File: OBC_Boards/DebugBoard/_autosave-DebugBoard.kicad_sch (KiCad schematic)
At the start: 15 parts, among them J1 Conn_01x02_Female, J2 Conn_02x06_Counter_Clockwise, J3 Conn_01x03, P1 USB_C_Plug_USB2.0, U1 L102021MS02Q

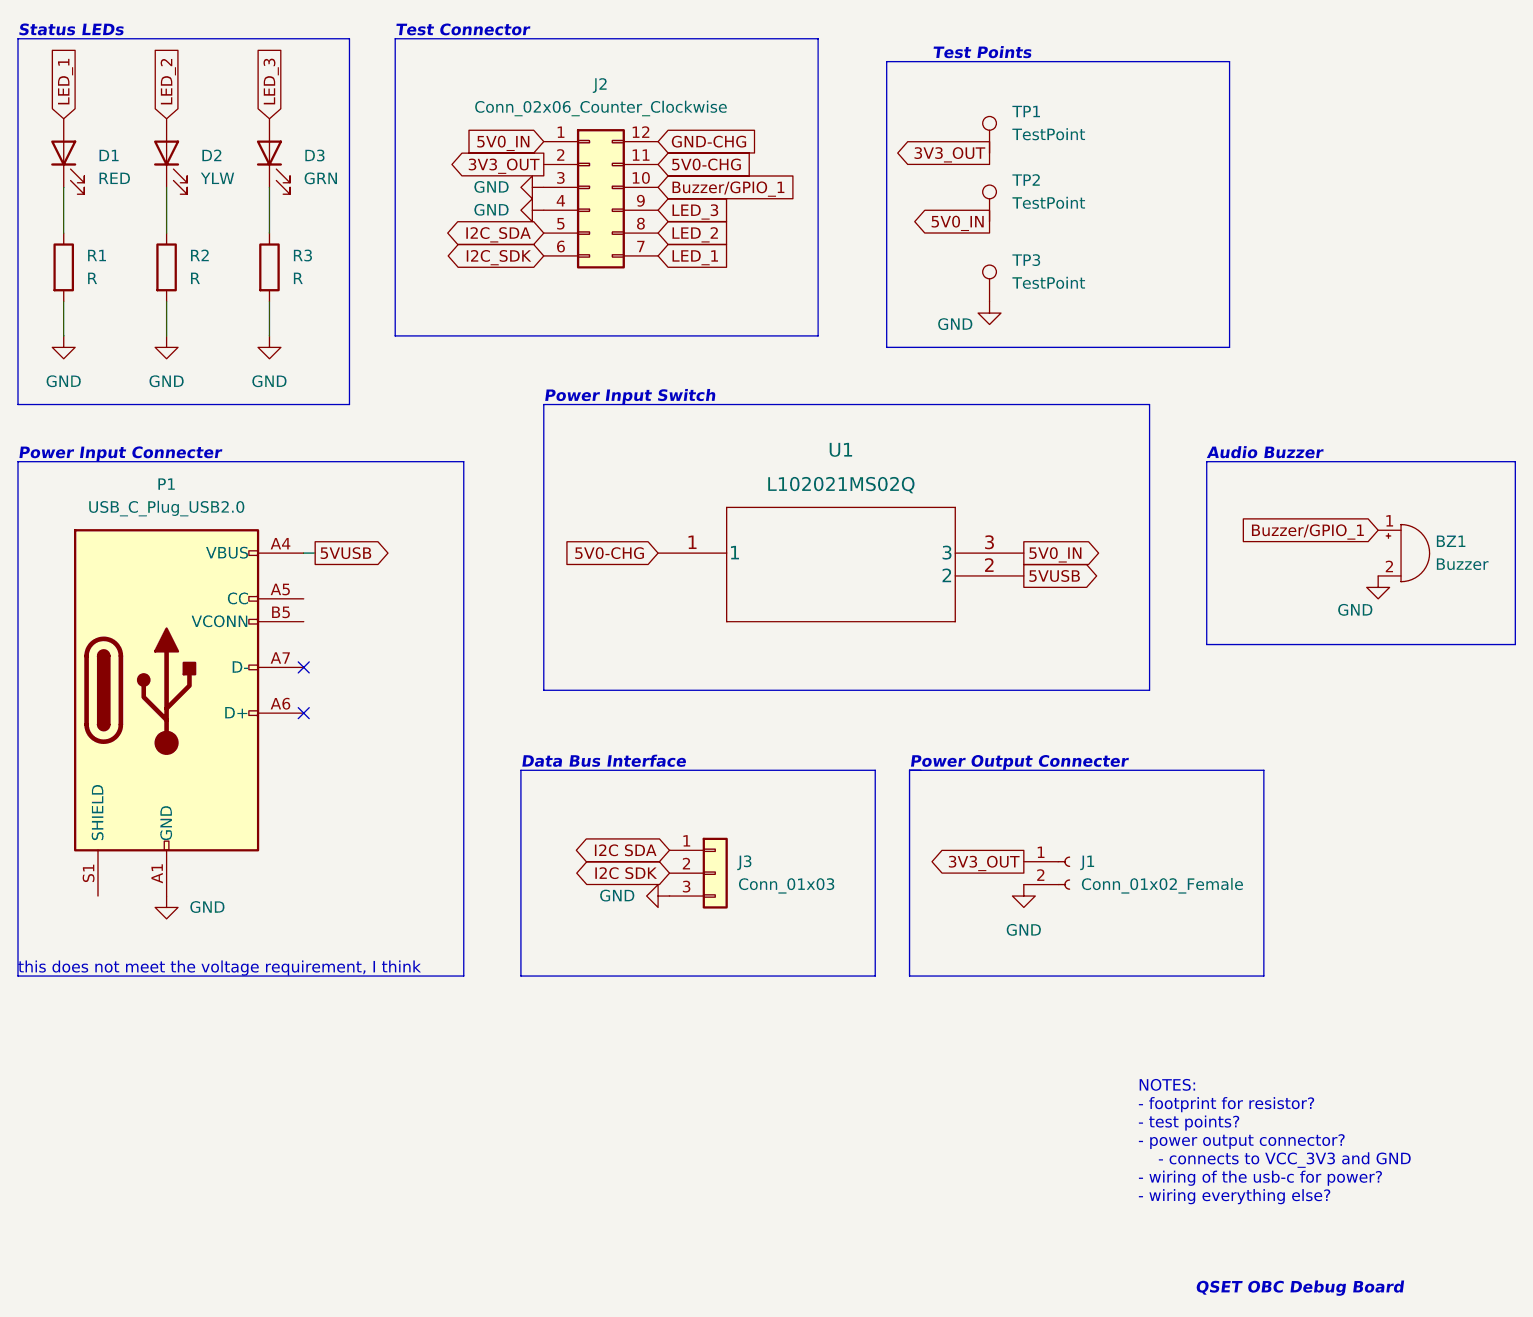
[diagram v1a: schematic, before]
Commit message: Created Debug PCB
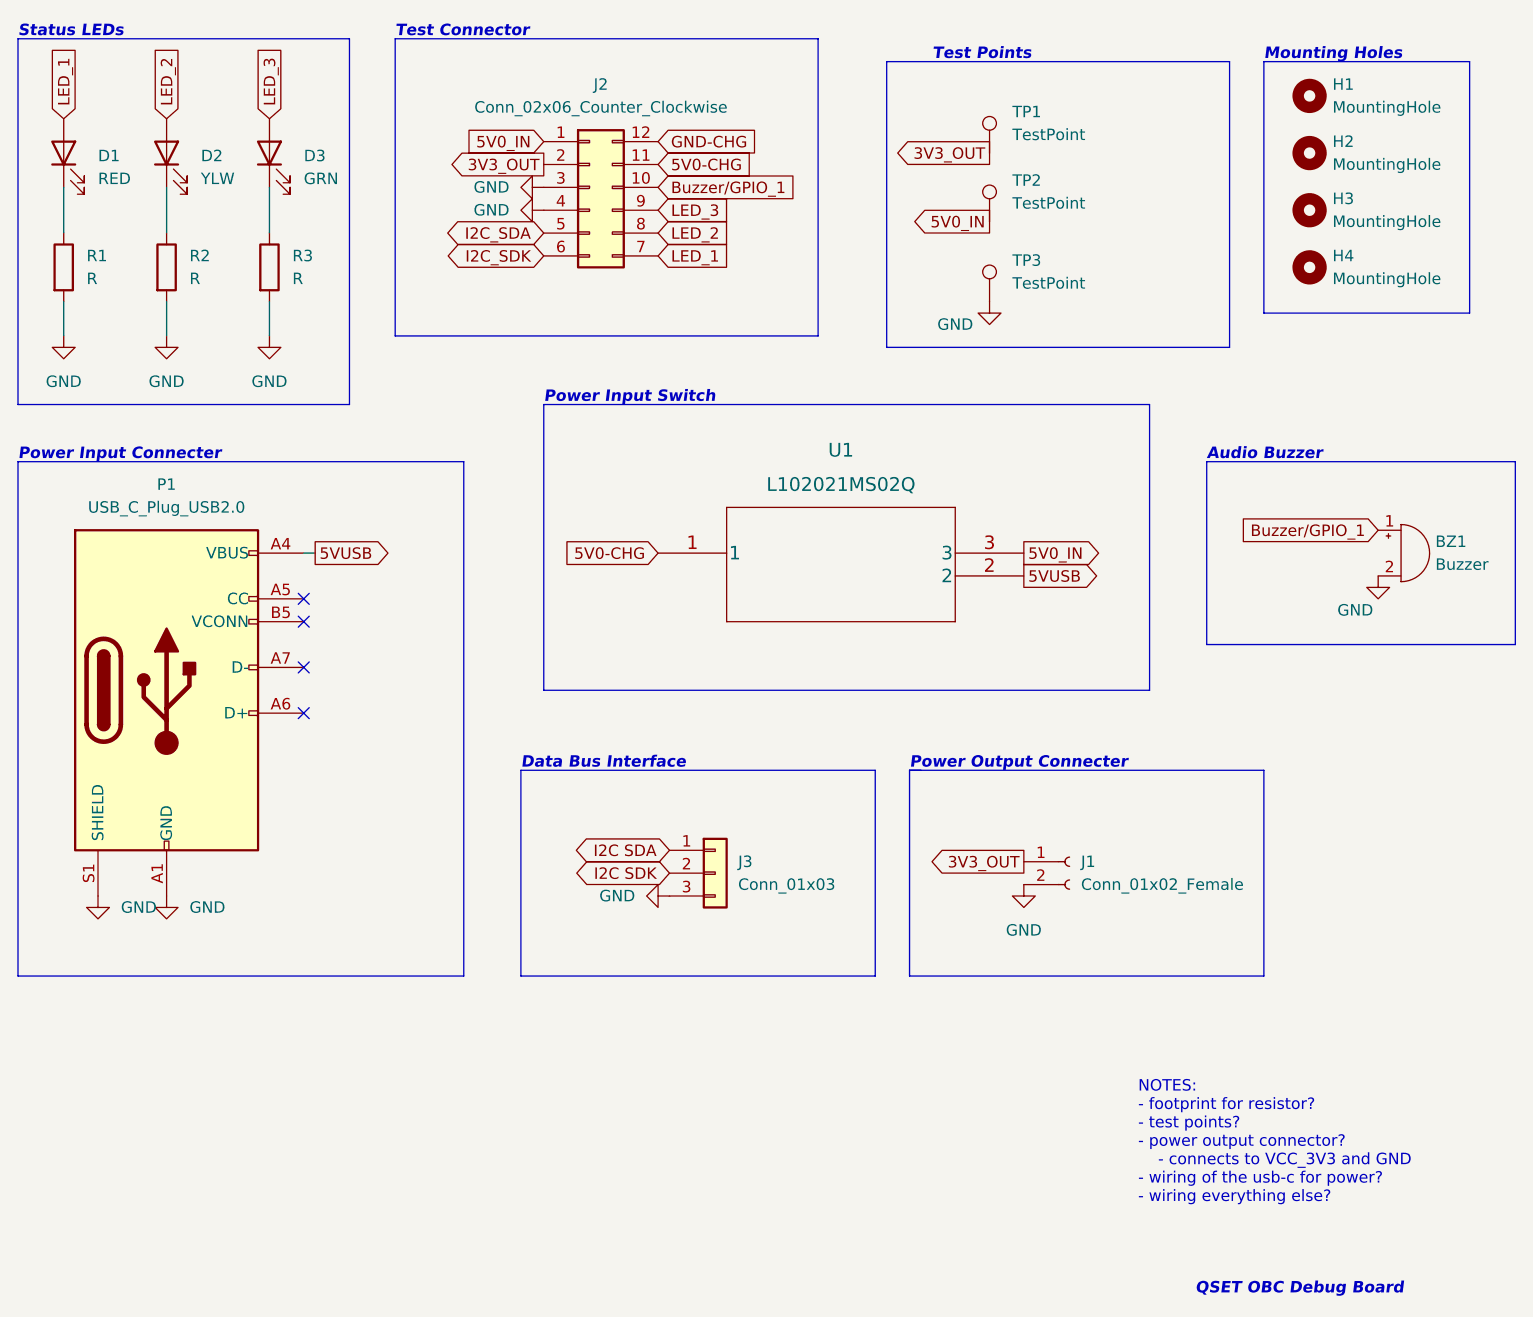
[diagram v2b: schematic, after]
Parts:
- added H1, H2, H3, H4: MountingHole, MountingHole:MountingHole_2.2mm_M2_Pad, symbol Mechanical:MountingHole
- J3: footprint (none) -> Connector_PinHeader_2.54mm:PinHeader_1x03_P2.54mm_Horizontal
- P1: footprint Connector_USB:USB_C_Receptacle_JAE_DX07S016JA1R1500 -> Connector_USB:USB_C_Receptacle_GCT_USB4085
- TP1: footprint (none) -> TestPoint:TestPoint_Pad_2.0x2.0mm
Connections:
- net GND: now also P1.S1 (SHIELD)
- no-connect marks 2 -> 4
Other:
- note added: "Mounting Holes"
- note removed: "this does not meet the voltage requirement, I think"
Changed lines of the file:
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@@
   (paper "A4")
   (no_connect (at 87.63 125.73))
+  (no_connect (at 87.63 115.57))
+  (no_connect (at 87.63 113.03))
   (no_connect (at 87.63 120.65))
   (polyline (pts (xy 154.94 132.08) (xy 156.21 132.08))
     (stroke (width 0) (type default) (color 0 0 0 0))
   )
+  (polyline (pts (xy 194.31 53.34) (xy 194.31 81.28))
+    (stroke (width 0) (type default) (color 0 0 0 0))
+  )
   (polyline (pts (xy 187.96 97.79) (xy 222.25 97.79))
     (stroke (width 0) (type default) (color 0 0 0 0))
@@
     (stroke (width 0) (type default) (color 0 0 0 0))
   )
+  (polyline (pts (xy 217.17 81.28) (xy 194.31 81.28))
+    (stroke (width 0) (type default) (color 0 0 0 0))
+  )
   (wire (pts (xy 72.39 67.31) (xy 72.39 72.39))
     (stroke (width 0) (type default) (color 0 0 0 0))
   )
+  (polyline (pts (xy 217.17 53.34) (xy 217.17 81.28))
+    (stroke (width 0) (type default) (color 0 0 0 0))
+  )
   (polyline (pts (xy 194.31 132.08) (xy 194.31 154.94))
     (stroke (width 0) (type default) (color 0 0 0 0))
@@
   )
   (polyline (pts (xy 111.76 132.08) (xy 151.13 132.08))
+    (stroke (width 0) (type default) (color 0 0 0 0))
+  )
+  (polyline (pts (xy 194.31 53.34) (xy 217.17 53.34))
     (stroke (width 0) (type default) (color 0 0 0 0))
   )
@@
   )
   (text "Power Input Switch\n" (at 114.3 91.44 0)
+    (effects (font (size 1.27 1.27) (thickness 0.254) bold italic) (justify left bottom))
+  )
+  (text "Mounting Holes" (at 194.31 53.34 0)
     (effects (font (size 1.27 1.27) (thickness 0.254) bold italic) (justify left bottom))
   )
@@
     (effects (font (size 1.27 1.27)) (justify left bottom))
   )
-  (text "this does not meet the voltage requirement, I think"
-    (at 55.88 154.94 0)
-    (effects (font (size 1.27 1.27)) (justify left bottom))
-  )
   (text "Power Input Connecter" (at 55.88 97.79 0)
     (effects (font (size 1.27 1.27) (thickness 0.254) bold italic) (justify left bottom))
@@
       (effects (font (size 1.27 1.27)) (justify left))
     )
-    (property "Footprint" "" (id 2) (at 168.91 63.5 0)
+    (property "Footprint" "TestPoint:TestPoint_Pad_2.0x2.0mm" (id 2) (at 168.91 63.5 0)
       (effects (font (size 1.27 1.27)) hide)
     )
@@
       (effects (font (size 1.27 1.27)) (justify left))
     )
-    (property "Footprint" "" (id 2) (at 133.35 143.51 0)
+    (property "Footprint" "Connector_PinHeader_2.54mm:PinHeader_1x03_P2.54mm_Horizontal" (id 2) (at 133.35 143.51 0)
       (effects (font (size 1.27 1.27)) hide)
     )
@@
     (property "Reference" "P1" (id 0) (at 72.39 100.33 0))
     (property "Value" "USB_C_Plug_USB2.0" (id 1) (at 72.39 102.87 0))
-    (property "Footprint" "Connector_USB:USB_C_Receptacle_JAE_DX07S016JA1R1500" (id 2) (at 76.2 123.19 0)
+    (property "Footprint" "Connector_USB:USB_C_Receptacle_GCT_USB4085" (id 2) (at 76.2 123.19 0)
       (effects (font (size 1.27 1.27)) hide)
     )
@@
     (pin "2")
   )
+  (symbol (lib_id "power:GND") (at 64.77 146.05 0) (unit 1)
+    (in_bom yes) (on_board yes) (fields_autoplaced)
+    (property "Reference" "#PWR0102" (id 0) (at 64.77 152.4 0)
+      (effects (font (size 1.27 1.27)) hide)
+    )
+    (property "Value" "GND" (id 1) (at 67.31 147.3199 0)
+      (effects (font (size 1.27 1.27)) (justify left))
+    )
+    (property "Footprint" "" (id 2) (at 64.77 146.05 0)
+      (effects (font (size 1.27 1.27)) hide)
+    )
+    (property "Datasheet" "" (id 3) (at 64.77 146.05 0)
+      (effects (font (size 1.27 1.27)) hide)
+    )
+    (pin "1")
+  )
+  (symbol (lib_id "Mechanical:MountingHole") (at 199.39 57.15 0) (unit 1)
+    (in_bom yes) (on_board yes) (fields_autoplaced)
+    (property "Reference" "H1" (id 0) (at 201.93 55.8799 0)
+      (effects (font (size 1.27 1.27)) (justify left))
+    )
+    (property "Value" "MountingHole" (id 1) (at 201.93 58.4199 0)
+      (effects (font (size 1.27 1.27)) (justify left))
+    )
+    (property "Footprint" "MountingHole:MountingHole_2.2mm_M2_Pad" (id 2) (at 199.39 57.15 0)
+      (effects (font (size 1.27 1.27)) hide)
+    )
+    (property "Datasheet" "~" (id 3) (at 199.39 57.15 0)
+      (effects (font (size 1.27 1.27)) hide)
+    )
+  )
   (symbol (lib_id "power:GND") (at 128.27 146.05 270) (unit 1)
     (in_bom yes) (on_board yes) (fields_autoplaced)
@@
     (pin "1")
   )
+  (symbol (lib_id "Mechanical:MountingHole") (at 199.39 63.5 0) (unit 1)
+    (in_bom yes) (on_board yes) (fields_autoplaced)
+    (property "Reference" "H2" (id 0) (at 201.93 62.2299 0)
+      (effects (font (size 1.27 1.27)) (justify left))
+    )
+    (property "Value" "MountingHole" (id 1) (at 201.93 64.7699 0)
+      (effects (font (size 1.27 1.27)) (justify left))
+    )
+    (property "Footprint" "MountingHole:MountingHole_2.2mm_M2_Pad" (id 2) (at 199.39 63.5 0)
+      (effects (font (size 1.27 1.27)) hide)
+    )
+    (property "Datasheet" "~" (id 3) (at 199.39 63.5 0)
+      (effects (font (size 1.27 1.27)) hide)
+    )
+  )
   (symbol (lib_id "Device:LED") (at 83.82 63.5 90) (unit 1)
     (in_bom yes) (on_board yes) (fields_autoplaced)
@@
     (pin "1")
     (pin "2")
+  )
+  (symbol (lib_id "Mechanical:MountingHole") (at 199.39 69.85 0) (unit 1)
+    (in_bom yes) (on_board yes) (fields_autoplaced)
+    (property "Reference" "H3" (id 0) (at 201.93 68.5799 0)
+      (effects (font (size 1.27 1.27)) (justify left))
+    )
+    (property "Value" "MountingHole" (id 1) (at 201.93 71.1199 0)
+      (effects (font (size 1.27 1.27)) (justify left))
+    )
+    (property "Footprint" "MountingHole:MountingHole_2.2mm_M2_Pad" (id 2) (at 199.39 69.85 0)
+      (effects (font (size 1.27 1.27)) hide)
+    )
+    (property "Datasheet" "~" (id 3) (at 199.39 69.85 0)
+      (effects (font (size 1.27 1.27)) hide)
+    )
   )
   (symbol (lib_id "power:GND") (at 60.96 83.82 0) (unit 1)
@@
     (pin "1")
   )
+  (symbol (lib_id "Mechanical:MountingHole") (at 199.39 76.2 0) (unit 1)
+    (in_bom yes) (on_board yes) (fields_autoplaced)
+    (property "Reference" "H4" (id 0) (at 201.93 74.9299 0)
+      (effects (font (size 1.27 1.27)) (justify left))
+    )
+    (property "Value" "MountingHole" (id 1) (at 201.93 77.4699 0)
+      (effects (font (size 1.27 1.27)) (justify left))
+    )
+    (property "Footprint" "MountingHole:MountingHole_2.2mm_M2_Pad" (id 2) (at 199.39 76.2 0)
+      (effects (font (size 1.27 1.27)) hide)
+    )
+    (property "Datasheet" "~" (id 3) (at 199.39 76.2 0)
+      (effects (font (size 1.27 1.27)) hide)
+    )
+  )
   (sheet_instances
     (path "/" (page "1"))
@@
       (reference "#PWR0101") (unit 1) (value "GND") (footprint "")
     )
+    (path "/910a7cb6-49a4-4cba-9031-90b91a99d687"
+      (reference "#PWR0102") (unit 1) (value "GND") (footprint "")
+    )
     (path "/6d0917a8-d0e4-4837-95b2-0a8ab01999fa"
       (reference "BZ1") (unit 1) (value "Buzzer") (footprint "Daughterboard_footprints:XDCR_CMT-8504-100-SMT-TR")
@@
       (reference "D3") (unit 1) (value "GRN") (footprint "LED_THT:LED_D3.0mm")
     )
+    (path "/96645670-7075-4809-b0bf-d8d6715b9631"
+      (reference "H1") (unit 1) (value "MountingHole") (footprint "MountingHole:MountingHole_2.2mm_M2_Pad")
+    )
+    (path "/a29aa068-d46a-4741-88a0-bdee67246c1a"
+      (reference "H2") (unit 1) (value "MountingHole") (footprint "MountingHole:MountingHole_2.2mm_M2_Pad")
+    )
+    (path "/bad90990-2ce7-4ee3-90fb-ff939f81a2f8"
+      (reference "H3") (unit 1) (value "MountingHole") (footprint "MountingHole:MountingHole_2.2mm_M2_Pad")
+    )
+    (path "/fa24c3bc-20df-4597-b783-977de3455d95"
+      (reference "H4") (unit 1) (value "MountingHole") (footprint "MountingHole:MountingHole_2.2mm_M2_Pad")
+    )
     (path "/2f4e69f3-a308-4903-b430-d023c23b2a3f"
       (reference "J1") (unit 1) (value "Conn_01x02_Female") (footprint "Connector_PinSocket_2.54mm:PinSocket_1x02_P2.54mm_Horizontal")
@@
     )
     (path "/1a72c237-7be8-4494-b633-765ee4f07660"
-      (reference "J3") (unit 1) (value "Conn_01x03") (footprint "")
+      (reference "J3") (unit 1) (value "Conn_01x03") (footprint "Connector_PinHeader_2.54mm:PinHeader_1x03_P2.54mm_Horizontal")
     )
     (path "/677d93ba-e4e6-40d2-b6d9-0ff4a4577d8b"
-      (reference "P1") (unit 1) (value "USB_C_Plug_USB2.0") (footprint "Connector_USB:USB_C_Receptacle_JAE_DX07S016JA1R1500")
+      (reference "P1") (unit 1) (value "USB_C_Plug_USB2.0") (footprint "Connector_USB:USB_C_Receptacle_GCT_USB4085")
     )
     (path "/5f848bab-73be-472a-9d63-31af9d9e1cf9"
@@
     )
     (path "/1646d695-b002-475a-8245-fc069803d803"
-      (reference "TP1") (unit 1) (value "TestPoint") (footprint "")
+      (reference "TP1") (unit 1) (value "TestPoint") (footprint "TestPoint:TestPoint_Pad_2.0x2.0mm")
     )
     (path "/a0395d07-65f8-4c65-a9d0-f3e64c260792"
